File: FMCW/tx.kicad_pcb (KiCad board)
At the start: 2 copper layers, 125 x 45 mm, 70 parts, among them J1 Barrel_Jack, J2 SMA_RX, J3 SMA_TX, J4 Conn_01x06_Male, U1 ADF4158, U10 HMC431LP4, U2 LP2985-3.3, U3 TLV172DCK, U4 LM1117-5.0, U5 LP2985-10.0, U6 LP2985-3.0, U7 SE5003_1, U8 TCXO

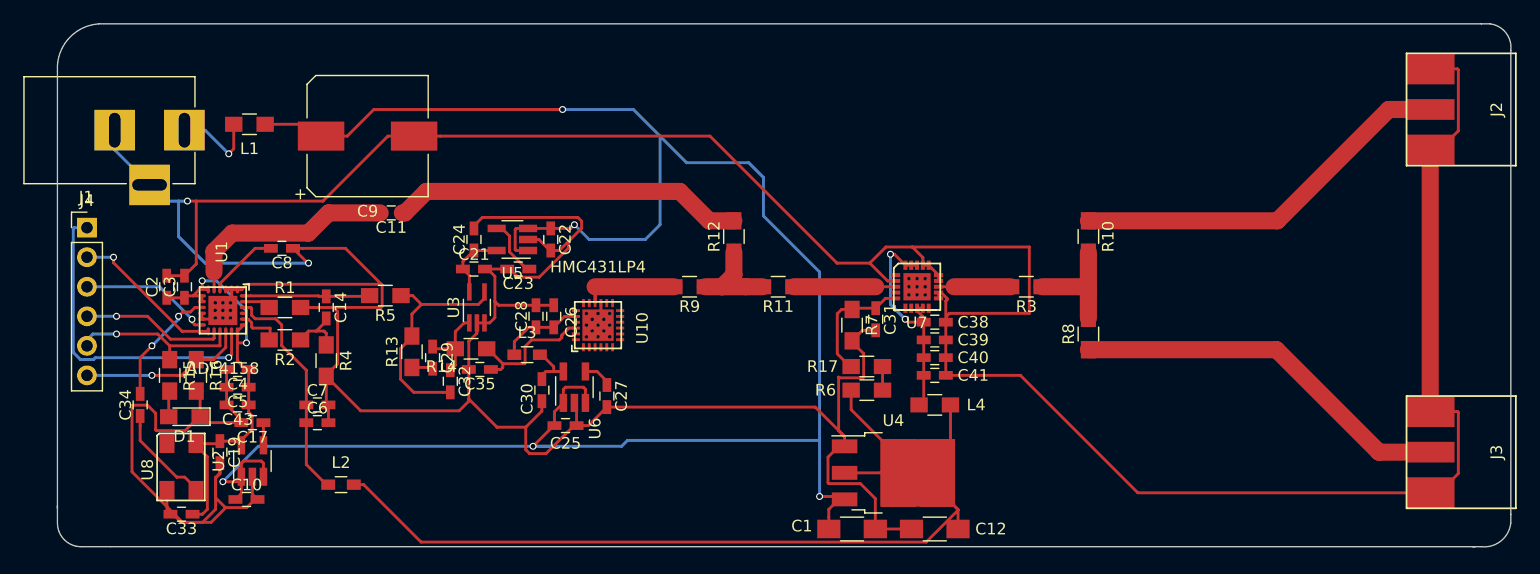
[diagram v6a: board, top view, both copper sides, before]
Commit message: Updated pcb with vias
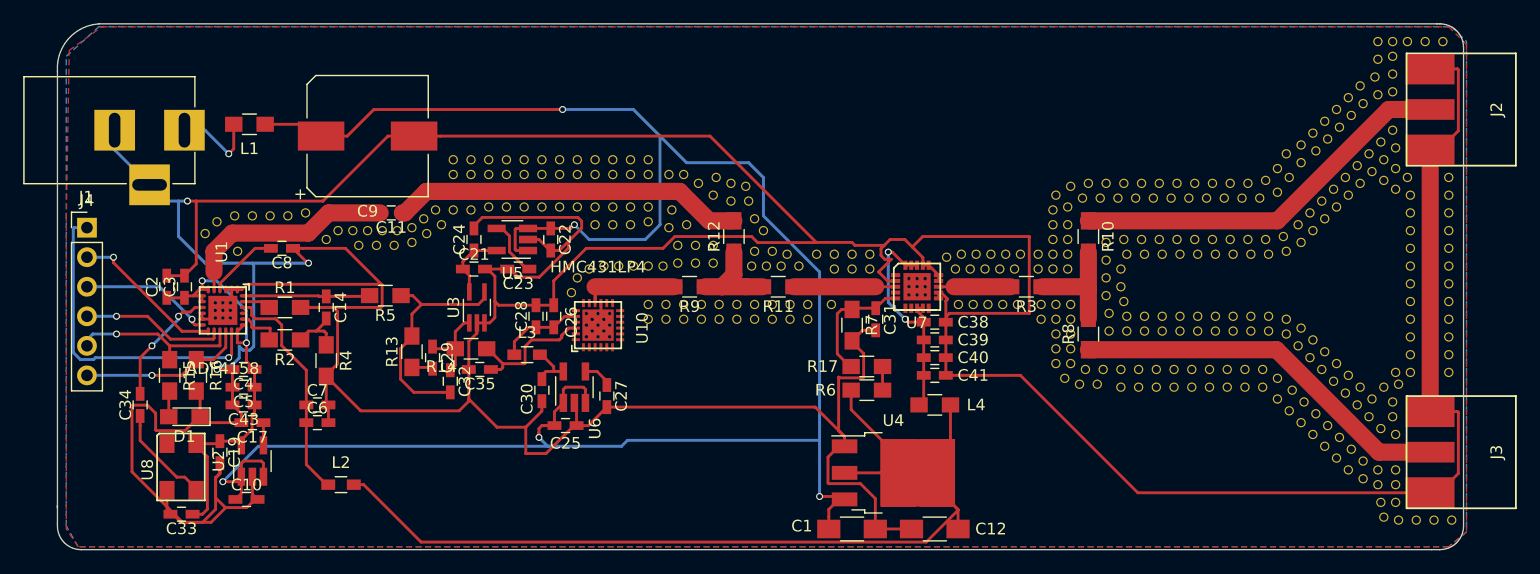
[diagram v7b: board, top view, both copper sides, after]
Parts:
- added REF**: VIA0.6mm, buradar:VIA0.6mm, F.Cu at (202.2, 91.2)
- added REF**: VIA0.6mm, buradar:VIA0.6mm, F.Cu at (190.2, 96.3)
- added REF**: VIA0.6mm, buradar:VIA0.6mm, F.Cu at (145.8, 97.3)
- added REF**: VIA0.6mm, buradar:VIA0.6mm, F.Cu at (147.1, 98.6)
- added REF**: VIA0.6mm, buradar:VIA0.6mm, F.Cu at (145.5, 98.8)
- added REF**: VIA0.6mm, buradar:VIA0.6mm, F.Cu at (150.9, 96.5)
- added REF**: VIA0.6mm, buradar:VIA0.6mm, F.Cu at (152.4, 96.5)
- added REF**: VIA0.6mm, buradar:VIA0.6mm, F.Cu at (149.6, 94.5)
- added REF**: VIA0.6mm, buradar:VIA0.6mm, F.Cu at (150.9, 95.0)
- added REF**: VIA0.6mm, buradar:VIA0.6mm, F.Cu at (152.1, 95.2)
- added REF**: VIA0.6mm, buradar:VIA0.6mm, F.Cu at (152.9, 98.0)
- added REF**: VIA0.6mm, buradar:VIA0.6mm, F.Cu at (153.7, 99.1)
- added REF**: VIA0.6mm, buradar:VIA0.6mm, F.Cu at (188.7, 96.3)
- added REF**: VIA0.6mm, buradar:VIA0.6mm, F.Cu at (152.9, 100.8)
- added REF**: VIA0.6mm, buradar:VIA0.6mm, F.Cu at (154.4, 100.8)
- added REF**: VIA0.6mm, buradar:VIA0.6mm, F.Cu at (156.7, 102.1)
- added REF**: VIA0.6mm, buradar:VIA0.6mm, F.Cu at (155.2, 102.1)
- added REF**: VIA0.6mm, buradar:VIA0.6mm, F.Cu at (153.9, 102.1)
- added REF**: VIA0.6mm, buradar:VIA0.6mm, F.Cu at (152.7, 102.1)
- added REF**: VIA0.6mm, buradar:VIA0.6mm, F.Cu at (155.7, 101.1)
- added REF**: VIA0.6mm, buradar:VIA0.6mm, F.Cu at (162.8, 102.4)
- added REF**: VIA0.6mm, buradar:VIA0.6mm, F.Cu at (161.3, 102.4)
- added REF**: VIA0.6mm, buradar:VIA0.6mm, F.Cu at (159.8, 102.4)
- added REF**: VIA0.6mm, buradar:VIA0.6mm, F.Cu at (187.2, 96.3)
- added REF**: VIA0.6mm, buradar:VIA0.6mm, F.Cu at (162.8, 101.1)
- added REF**: VIA0.6mm, buradar:VIA0.6mm, F.Cu at (161.3, 101.1)
- added REF**: VIA0.6mm, buradar:VIA0.6mm, F.Cu at (159.8, 101.1)
- added REF**: VIA0.6mm, buradar:VIA0.6mm, F.Cu at (158.2, 101.1)
- added REF**: VIA0.6mm, buradar:VIA0.6mm, F.Cu at (159.5, 105.4)
- added REF**: VIA0.6mm, buradar:VIA0.6mm, F.Cu at (157.5, 105.4)
- added REF**: VIA0.6mm, buradar:VIA0.6mm, F.Cu at (156.0, 105.4)
- added REF**: VIA0.6mm, buradar:VIA0.6mm, F.Cu at (154.4, 105.4)
- added REF**: VIA0.6mm, buradar:VIA0.6mm, F.Cu at (152.9, 105.4)
- added REF**: VIA0.6mm, buradar:VIA0.6mm, F.Cu at (151.4, 105.4)
- added REF**: VIA0.6mm, buradar:VIA0.6mm, F.Cu at (185.7, 96.3)
- added REF**: VIA0.6mm, buradar:VIA0.6mm, F.Cu at (149.9, 105.4)
- added REF**: VIA0.6mm, buradar:VIA0.6mm, F.Cu at (148.3, 105.4)
- added REF**: VIA0.6mm, buradar:VIA0.6mm, F.Cu at (146.8, 105.4)
- added REF**: VIA0.6mm, buradar:VIA0.6mm, F.Cu at (145.3, 105.4)
- added REF**: VIA0.6mm, buradar:VIA0.6mm, F.Cu at (143.8, 105.4)
- added REF**: VIA0.6mm, buradar:VIA0.6mm, F.Cu at (143.8, 106.7)
- added REF**: VIA0.6mm, buradar:VIA0.6mm, F.Cu at (145.3, 106.7)
- added REF**: VIA0.6mm, buradar:VIA0.6mm, F.Cu at (146.8, 106.7)
- added REF**: VIA0.6mm, buradar:VIA0.6mm, F.Cu at (148.3, 106.7)
- added REF**: VIA0.6mm, buradar:VIA0.6mm, F.Cu at (149.9, 106.7)
- added REF**: VIA0.6mm, buradar:VIA0.6mm, F.Cu at (184.2, 96.3)
- added REF**: VIA0.6mm, buradar:VIA0.6mm, F.Cu at (151.4, 106.7)
- added REF**: VIA0.6mm, buradar:VIA0.6mm, F.Cu at (152.9, 106.7)
- added REF**: VIA0.6mm, buradar:VIA0.6mm, F.Cu at (154.4, 106.7)
- added REF**: VIA0.6mm, buradar:VIA0.6mm, F.Cu at (156.0, 106.7)
- added REF**: VIA0.6mm, buradar:VIA0.6mm, F.Cu at (157.5, 106.7)
- added REF**: VIA0.6mm, buradar:VIA0.6mm, F.Cu at (170.2, 102.4)
- added REF**: VIA0.6mm, buradar:VIA0.6mm, F.Cu at (171.4, 102.4)
- added REF**: VIA0.6mm, buradar:VIA0.6mm, F.Cu at (172.7, 102.4)
- added REF**: VIA0.6mm, buradar:VIA0.6mm, F.Cu at (174.0, 102.4)
- added REF**: VIA0.6mm, buradar:VIA0.6mm, F.Cu at (175.3, 102.4)
- added REF**: VIA0.6mm, buradar:VIA0.6mm, F.Cu at (182.6, 96.3)
- added REF**: VIA0.6mm, buradar:VIA0.6mm, F.Cu at (169.4, 101.3)
- added REF**: VIA0.6mm, buradar:VIA0.6mm, F.Cu at (170.7, 101.1)
- added REF**: VIA0.6mm, buradar:VIA0.6mm, F.Cu at (172.0, 101.1)
- added REF**: VIA0.6mm, buradar:VIA0.6mm, F.Cu at (173.2, 101.1)
- added REF**: VIA0.6mm, buradar:VIA0.6mm, F.Cu at (174.5, 101.1)
- added REF**: VIA0.6mm, buradar:VIA0.6mm, F.Cu at (175.8, 101.1)
- added REF**: VIA0.6mm, buradar:VIA0.6mm, F.Cu at (170.4, 105.4)
- added REF**: VIA0.6mm, buradar:VIA0.6mm, F.Cu at (171.7, 105.4)
- added REF**: VIA0.6mm, buradar:VIA0.6mm, F.Cu at (173.0, 105.4)
- added REF**: VIA0.6mm, buradar:VIA0.6mm, F.Cu at (174.2, 105.4)
- added REF**: VIA0.6mm, buradar:VIA0.6mm, F.Cu at (181.1, 96.3)
- added REF**: VIA0.6mm, buradar:VIA0.6mm, F.Cu at (175.5, 105.4)
- added REF**: VIA0.6mm, buradar:VIA0.6mm, F.Cu at (177.3, 102.4)
- added REF**: VIA0.6mm, buradar:VIA0.6mm, F.Cu at (178.6, 102.4)
- added REF**: VIA0.6mm, buradar:VIA0.6mm, F.Cu at (179.8, 102.4)
- added REF**: VIA0.6mm, buradar:VIA0.6mm, F.Cu at (179.8, 101.1)
- added REF**: VIA0.6mm, buradar:VIA0.6mm, F.Cu at (178.6, 101.1)
- added REF**: VIA0.6mm, buradar:VIA0.6mm, F.Cu at (177.3, 101.1)
- added REF**: VIA0.6mm, buradar:VIA0.6mm, F.Cu at (179.8, 99.8)
- added REF**: VIA0.6mm, buradar:VIA0.6mm, F.Cu at (179.8, 98.6)
- added REF**: VIA0.6mm, buradar:VIA0.6mm, F.Cu at (179.8, 97.0)
- added REF**: VIA0.6mm, buradar:VIA0.6mm, F.Cu at (200.9, 90.7)
- added REF**: VIA0.6mm, buradar:VIA0.6mm, F.Cu at (178.6, 99.8)
- added REF**: VIA0.6mm, buradar:VIA0.6mm, F.Cu at (178.6, 98.6)
- added REF**: VIA0.6mm, buradar:VIA0.6mm, F.Cu at (178.6, 97.3)
- added REF**: VIA0.6mm, buradar:VIA0.6mm, F.Cu at (178.8, 96.0)
- added REF**: VIA0.6mm, buradar:VIA0.6mm, F.Cu at (149.4, 100.3)
- added REF**: VIA0.6mm, buradar:VIA0.6mm, F.Cu at (149.4, 101.9)
- added REF**: VIA0.6mm, buradar:VIA0.6mm, F.Cu at (147.8, 101.9)
- added REF**: VIA0.6mm, buradar:VIA0.6mm, F.Cu at (147.8, 100.3)
- added REF**: VIA0.6mm, buradar:VIA0.6mm, F.Cu at (146.3, 100.3)
- added REF**: VIA0.6mm, buradar:VIA0.6mm, F.Cu at (146.3, 101.9)
- added REF**: VIA0.6mm, buradar:VIA0.6mm, F.Cu at (199.9, 91.7)
- added REF**: VIA0.6mm, buradar:VIA0.6mm, F.Cu at (145.0, 102.1)
- added REF**: VIA0.6mm, buradar:VIA0.6mm, F.Cu at (143.8, 102.1)
- added REF**: VIA0.6mm, buradar:VIA0.6mm, F.Cu at (142.5, 102.1)
- added REF**: VIA0.6mm, buradar:VIA0.6mm, F.Cu at (141.2, 102.1)
- added REF**: VIA0.6mm, buradar:VIA0.6mm, F.Cu at (140.0, 102.1)
- added REF**: VIA0.6mm, buradar:VIA0.6mm, F.Cu at (138.7, 102.4)
- added REF**: VIA0.6mm, buradar:VIA0.6mm, F.Cu at (137.7, 103.1)
- added REF**: VIA0.6mm, buradar:VIA0.6mm, F.Cu at (137.2, 104.4)
- added REF**: VIA0.6mm, buradar:VIA0.6mm, F.Cu at (180.1, 105.4)
- added REF**: VIA0.6mm, buradar:VIA0.6mm, F.Cu at (178.8, 105.4)
- added REF**: VIA0.6mm, buradar:VIA0.6mm, F.Cu at (198.6, 92.5)
- added REF**: VIA0.6mm, buradar:VIA0.6mm, F.Cu at (177.5, 105.4)
- added REF**: VIA0.6mm, buradar:VIA0.6mm, F.Cu at (177.5, 106.7)
- added REF**: VIA0.6mm, buradar:VIA0.6mm, F.Cu at (178.8, 106.7)
- added REF**: VIA0.6mm, buradar:VIA0.6mm, F.Cu at (180.1, 106.7)
- added REF**: VIA0.6mm, buradar:VIA0.6mm, F.Cu at (180.1, 108.0)
- added REF**: VIA0.6mm, buradar:VIA0.6mm, F.Cu at (180.1, 109.2)
- added REF**: VIA0.6mm, buradar:VIA0.6mm, F.Cu at (180.1, 110.5)
- added REF**: VIA0.6mm, buradar:VIA0.6mm, F.Cu at (178.8, 108.0)
- added REF**: VIA0.6mm, buradar:VIA0.6mm, F.Cu at (178.8, 109.2)
- added REF**: VIA0.6mm, buradar:VIA0.6mm, F.Cu at (178.8, 110.5)
- added REF**: VIA0.6mm, buradar:VIA0.6mm, F.Cu at (201.2, 92.2)
- added REF**: VIA0.6mm, buradar:VIA0.6mm, F.Cu at (197.9, 93.7)
- added REF**: VIA0.6mm, buradar:VIA0.6mm, F.Cu at (181.4, 111.0)
- added REF**: VIA0.6mm, buradar:VIA0.6mm, F.Cu at (182.9, 111.0)
- added REF**: VIA0.6mm, buradar:VIA0.6mm, F.Cu at (179.6, 111.8)
- added REF**: VIA0.6mm, buradar:VIA0.6mm, F.Cu at (180.8, 112.3)
- added REF**: VIA0.6mm, buradar:VIA0.6mm, F.Cu at (182.4, 112.3)
- added REF**: VIA0.6mm, buradar:VIA0.6mm, F.Cu at (184.4, 111.0)
- added REF**: VIA0.6mm, buradar:VIA0.6mm, F.Cu at (185.9, 111.0)
- added REF**: VIA0.6mm, buradar:VIA0.6mm, F.Cu at (187.5, 111.0)
- added REF**: VIA0.6mm, buradar:VIA0.6mm, F.Cu at (189.0, 111.0)
- added REF**: VIA0.6mm, buradar:VIA0.6mm, F.Cu at (190.5, 111.0)
- added REF**: VIA0.6mm, buradar:VIA0.6mm, F.Cu at (196.8, 94.7)
- added REF**: VIA0.6mm, buradar:VIA0.6mm, F.Cu at (192.0, 111.0)
- added REF**: VIA0.6mm, buradar:VIA0.6mm, F.Cu at (193.5, 111.0)
- added REF**: VIA0.6mm, buradar:VIA0.6mm, F.Cu at (195.1, 111.0)
- added REF**: VIA0.6mm, buradar:VIA0.6mm, F.Cu at (196.6, 111.0)
- added REF**: VIA0.6mm, buradar:VIA0.6mm, F.Cu at (197.9, 111.8)
- added REF**: VIA0.6mm, buradar:VIA0.6mm, F.Cu at (199.1, 112.8)
- added REF**: VIA0.6mm, buradar:VIA0.6mm, F.Cu at (200.2, 113.8)
- added REF**: VIA0.6mm, buradar:VIA0.6mm, F.Cu at (201.2, 114.8)
- added REF**: VIA0.6mm, buradar:VIA0.6mm, F.Cu at (202.2, 115.8)
- added REF**: VIA0.6mm, buradar:VIA0.6mm, F.Cu at (203.2, 116.8)
- added REF**: VIA0.6mm, buradar:VIA0.6mm, F.Cu at (195.3, 95.0)
- added REF**: VIA0.6mm, buradar:VIA0.6mm, F.Cu at (204.2, 117.9)
- added REF**: VIA0.6mm, buradar:VIA0.6mm, F.Cu at (205.2, 118.9)
- added REF**: VIA0.6mm, buradar:VIA0.6mm, F.Cu at (206.5, 119.6)
- added REF**: VIA0.6mm, buradar:VIA0.6mm, F.Cu at (208.0, 119.6)
- added REF**: VIA0.6mm, buradar:VIA0.6mm, F.Cu at (208.0, 120.9)
- added REF**: VIA0.6mm, buradar:VIA0.6mm, F.Cu at (206.5, 120.9)
- added REF**: VIA0.6mm, buradar:VIA0.6mm, F.Cu at (205.2, 120.4)
- added REF**: VIA0.6mm, buradar:VIA0.6mm, F.Cu at (204.0, 119.6)
- added REF**: VIA0.6mm, buradar:VIA0.6mm, F.Cu at (202.9, 118.6)
- added REF**: VIA0.6mm, buradar:VIA0.6mm, F.Cu at (201.9, 117.6)
- added REF**: VIA0.6mm, buradar:VIA0.6mm, F.Cu at (193.8, 95.0)
- added REF**: VIA0.6mm, buradar:VIA0.6mm, F.Cu at (200.9, 116.6)
- added REF**: VIA0.6mm, buradar:VIA0.6mm, F.Cu at (199.9, 115.6)
- added REF**: VIA0.6mm, buradar:VIA0.6mm, F.Cu at (198.9, 114.6)
- added REF**: VIA0.6mm, buradar:VIA0.6mm, F.Cu at (197.9, 113.5)
- added REF**: VIA0.6mm, buradar:VIA0.6mm, F.Cu at (196.6, 112.5)
- added REF**: VIA0.6mm, buradar:VIA0.6mm, F.Cu at (195.1, 112.5)
- added REF**: VIA0.6mm, buradar:VIA0.6mm, F.Cu at (193.5, 112.5)
- added REF**: VIA0.6mm, buradar:VIA0.6mm, F.Cu at (192.0, 112.5)
- added REF**: VIA0.6mm, buradar:VIA0.6mm, F.Cu at (190.5, 112.5)
- added REF**: VIA0.6mm, buradar:VIA0.6mm, F.Cu at (189.0, 112.5)
- added REF**: VIA0.6mm, buradar:VIA0.6mm, F.Cu at (192.3, 95.0)
- added REF**: VIA0.6mm, buradar:VIA0.6mm, F.Cu at (187.5, 112.5)
- added REF**: VIA0.6mm, buradar:VIA0.6mm, F.Cu at (185.9, 112.5)
- added REF**: VIA0.6mm, buradar:VIA0.6mm, F.Cu at (184.4, 112.5)
- added REF**: VIA0.6mm, buradar:VIA0.6mm, F.Cu at (203.2, 90.2)
- added REF**: VIA0.6mm, buradar:VIA0.6mm, F.Cu at (204.2, 89.2)
- added REF**: VIA0.6mm, buradar:VIA0.6mm, F.Cu at (205.2, 88.1)
- added REF**: VIA0.6mm, buradar:VIA0.6mm, F.Cu at (206.5, 87.4)
- added REF**: VIA0.6mm, buradar:VIA0.6mm, F.Cu at (207.8, 87.1)
- added REF**: VIA0.6mm, buradar:VIA0.6mm, F.Cu at (212.1, 82.8)
- added REF**: VIA0.6mm, buradar:VIA0.6mm, F.Cu at (210.6, 82.8)
- added REF**: VIA0.6mm, buradar:VIA0.6mm, F.Cu at (190.8, 95.0)
- added REF**: VIA0.6mm, buradar:VIA0.6mm, F.Cu at (209.0, 82.8)
- added REF**: VIA0.6mm, buradar:VIA0.6mm, F.Cu at (201.9, 89.7)
- added REF**: VIA0.6mm, buradar:VIA0.6mm, F.Cu at (202.9, 88.6)
- added REF**: VIA0.6mm, buradar:VIA0.6mm, F.Cu at (204.0, 87.6)
- added REF**: VIA0.6mm, buradar:VIA0.6mm, F.Cu at (205.0, 86.6)
- added REF**: VIA0.6mm, buradar:VIA0.6mm, F.Cu at (206.2, 85.9)
- added REF**: VIA0.6mm, buradar:VIA0.6mm, F.Cu at (207.8, 85.6)
- added REF**: VIA0.6mm, buradar:VIA0.6mm, F.Cu at (207.8, 84.1)
- added REF**: VIA0.6mm, buradar:VIA0.6mm, F.Cu at (207.8, 82.8)
- added REF**: VIA0.6mm, buradar:VIA0.6mm, F.Cu at (206.5, 84.3)
- added REF**: VIA0.6mm, buradar:VIA0.6mm, F.Cu at (189.2, 95.0)
- added REF**: VIA0.6mm, buradar:VIA0.6mm, F.Cu at (206.5, 82.8)
- added REF**: VIA0.6mm, buradar:VIA0.6mm, F.Cu at (208.0, 122.4)
- added REF**: VIA0.6mm, buradar:VIA0.6mm, F.Cu at (212.9, 124.0)
- added REF**: VIA0.6mm, buradar:VIA0.6mm, F.Cu at (211.3, 124.0)
- added REF**: VIA0.6mm, buradar:VIA0.6mm, F.Cu at (209.8, 124.0)
- added REF**: VIA0.6mm, buradar:VIA0.6mm, F.Cu at (208.3, 124.0)
- added REF**: VIA0.6mm, buradar:VIA0.6mm, F.Cu at (206.8, 122.4)
- added REF**: VIA0.6mm, buradar:VIA0.6mm, F.Cu at (207.0, 123.7)
- added REF**: VIA0.6mm, buradar:VIA0.6mm, F.Cu at (212.6, 94.5)
- added REF**: VIA0.6mm, buradar:VIA0.6mm, F.Cu at (212.6, 96.0)
- added REF**: VIA0.6mm, buradar:VIA0.6mm, F.Cu at (187.7, 95.0)
- added REF**: VIA0.6mm, buradar:VIA0.6mm, F.Cu at (212.6, 97.5)
- added REF**: VIA0.6mm, buradar:VIA0.6mm, F.Cu at (212.6, 99.1)
- added REF**: VIA0.6mm, buradar:VIA0.6mm, F.Cu at (212.6, 100.6)
- added REF**: VIA0.6mm, buradar:VIA0.6mm, F.Cu at (212.6, 102.1)
- added REF**: VIA0.6mm, buradar:VIA0.6mm, F.Cu at (212.6, 103.6)
- added REF**: VIA0.6mm, buradar:VIA0.6mm, F.Cu at (212.6, 105.2)
- added REF**: VIA0.6mm, buradar:VIA0.6mm, F.Cu at (212.6, 106.7)
- added REF**: VIA0.6mm, buradar:VIA0.6mm, F.Cu at (212.6, 108.2)
- added REF**: VIA0.6mm, buradar:VIA0.6mm, F.Cu at (212.6, 109.7)
- added REF**: VIA0.6mm, buradar:VIA0.6mm, F.Cu at (212.6, 111.3)
- added REF**: VIA0.6mm, buradar:VIA0.6mm, F.Cu at (186.2, 95.0)
- added REF**: VIA0.6mm, buradar:VIA0.6mm, F.Cu at (207.8, 90.4)
- added REF**: VIA0.6mm, buradar:VIA0.6mm, F.Cu at (208.0, 91.9)
- added REF**: VIA0.6mm, buradar:VIA0.6mm, F.Cu at (207.0, 93.0)
- added REF**: VIA0.6mm, buradar:VIA0.6mm, F.Cu at (209.0, 94.5)
- added REF**: VIA0.6mm, buradar:VIA0.6mm, F.Cu at (209.3, 96.0)
- added REF**: VIA0.6mm, buradar:VIA0.6mm, F.Cu at (209.3, 97.5)
- added REF**: VIA0.6mm, buradar:VIA0.6mm, F.Cu at (209.3, 99.1)
- added REF**: VIA0.6mm, buradar:VIA0.6mm, F.Cu at (209.3, 100.6)
- added REF**: VIA0.6mm, buradar:VIA0.6mm, F.Cu at (209.3, 102.1)
- added REF**: VIA0.6mm, buradar:VIA0.6mm, F.Cu at (209.3, 103.6)
- added REF**: VIA0.6mm, buradar:VIA0.6mm, F.Cu at (184.7, 95.0)
- added REF**: VIA0.6mm, buradar:VIA0.6mm, F.Cu at (209.3, 105.2)
- added REF**: VIA0.6mm, buradar:VIA0.6mm, F.Cu at (209.3, 106.7)
- added REF**: VIA0.6mm, buradar:VIA0.6mm, F.Cu at (209.3, 108.2)
- added REF**: VIA0.6mm, buradar:VIA0.6mm, F.Cu at (209.3, 109.7)
- added REF**: VIA0.6mm, buradar:VIA0.6mm, F.Cu at (209.3, 111.3)
- added REF**: VIA0.6mm, buradar:VIA0.6mm, F.Cu at (208.3, 112.3)
- added REF**: VIA0.6mm, buradar:VIA0.6mm, F.Cu at (207.8, 113.8)
- added REF**: VIA0.6mm, buradar:VIA0.6mm, F.Cu at (207.8, 115.1)
- added REF**: VIA0.6mm, buradar:VIA0.6mm, F.Cu at (208.0, 116.6)
- added REF**: VIA0.6mm, buradar:VIA0.6mm, F.Cu at (206.8, 116.1)
- added REF**: VIA0.6mm, buradar:VIA0.6mm, F.Cu at (199.9, 93.2)
- added REF**: VIA0.6mm, buradar:VIA0.6mm, F.Cu at (183.1, 95.0)
- added REF**: VIA0.6mm, buradar:VIA0.6mm, F.Cu at (205.7, 115.1)
- added REF**: VIA0.6mm, buradar:VIA0.6mm, F.Cu at (204.7, 114.0)
- added REF**: VIA0.6mm, buradar:VIA0.6mm, F.Cu at (203.7, 113.0)
- added REF**: VIA0.6mm, buradar:VIA0.6mm, F.Cu at (202.7, 112.0)
- added REF**: VIA0.6mm, buradar:VIA0.6mm, F.Cu at (201.7, 111.0)
- added REF**: VIA0.6mm, buradar:VIA0.6mm, F.Cu at (200.7, 110.0)
- added REF**: VIA0.6mm, buradar:VIA0.6mm, F.Cu at (199.6, 109.0)
- added REF**: VIA0.6mm, buradar:VIA0.6mm, F.Cu at (198.6, 108.0)
- added REF**: VIA0.6mm, buradar:VIA0.6mm, F.Cu at (197.1, 107.7)
- added REF**: VIA0.6mm, buradar:VIA0.6mm, F.Cu at (195.6, 107.7)
- added REF**: VIA0.6mm, buradar:VIA0.6mm, F.Cu at (181.6, 95.0)
- added REF**: VIA0.6mm, buradar:VIA0.6mm, F.Cu at (194.1, 107.7)
- added REF**: VIA0.6mm, buradar:VIA0.6mm, F.Cu at (192.5, 107.7)
- added REF**: VIA0.6mm, buradar:VIA0.6mm, F.Cu at (191.0, 107.7)
- added REF**: VIA0.6mm, buradar:VIA0.6mm, F.Cu at (189.5, 107.7)
- added REF**: VIA0.6mm, buradar:VIA0.6mm, F.Cu at (188.0, 107.7)
- added REF**: VIA0.6mm, buradar:VIA0.6mm, F.Cu at (186.4, 107.7)
- added REF**: VIA0.6mm, buradar:VIA0.6mm, F.Cu at (184.9, 107.7)
- added REF**: VIA0.6mm, buradar:VIA0.6mm, F.Cu at (183.4, 107.7)
- added REF**: VIA0.6mm, buradar:VIA0.6mm, F.Cu at (183.4, 106.2)
- added REF**: VIA0.6mm, buradar:VIA0.6mm, F.Cu at (183.1, 104.6)
- added REF**: VIA0.6mm, buradar:VIA0.6mm, F.Cu at (180.1, 95.2)
- added REF**: VIA0.6mm, buradar:VIA0.6mm, F.Cu at (183.1, 103.1)
- added REF**: VIA0.6mm, buradar:VIA0.6mm, F.Cu at (183.1, 101.6)
- added REF**: VIA0.6mm, buradar:VIA0.6mm, F.Cu at (183.1, 100.1)
- added REF**: VIA0.6mm, buradar:VIA0.6mm, F.Cu at (184.7, 99.8)
- added REF**: VIA0.6mm, buradar:VIA0.6mm, F.Cu at (186.2, 99.8)
- added REF**: VIA0.6mm, buradar:VIA0.6mm, F.Cu at (187.7, 99.8)
- added REF**: VIA0.6mm, buradar:VIA0.6mm, F.Cu at (189.2, 99.8)
- added REF**: VIA0.6mm, buradar:VIA0.6mm, F.Cu at (190.8, 99.8)
- added REF**: VIA0.6mm, buradar:VIA0.6mm, F.Cu at (192.3, 99.8)
- added REF**: VIA0.6mm, buradar:VIA0.6mm, F.Cu at (193.8, 99.8)
- added REF**: VIA0.6mm, buradar:VIA0.6mm, F.Cu at (149.4, 96.0)
- added REF**: VIA0.6mm, buradar:VIA0.6mm, F.Cu at (195.3, 99.8)
- added REF**: VIA0.6mm, buradar:VIA0.6mm, F.Cu at (196.8, 99.8)
- added REF**: VIA0.6mm, buradar:VIA0.6mm, F.Cu at (198.4, 99.6)
- added REF**: VIA0.6mm, buradar:VIA0.6mm, F.Cu at (199.6, 98.6)
- added REF**: VIA0.6mm, buradar:VIA0.6mm, F.Cu at (200.7, 97.5)
- added REF**: VIA0.6mm, buradar:VIA0.6mm, F.Cu at (201.7, 96.5)
- added REF**: VIA0.6mm, buradar:VIA0.6mm, F.Cu at (202.7, 95.5)
- added REF**: VIA0.6mm, buradar:VIA0.6mm, F.Cu at (203.7, 94.5)
- added REF**: VIA0.6mm, buradar:VIA0.6mm, F.Cu at (204.7, 93.5)
- added REF**: VIA0.6mm, buradar:VIA0.6mm, F.Cu at (205.7, 92.5)
- added REF**: VIA0.6mm, buradar:VIA0.6mm, F.Cu at (148.1, 95.0)
- added REF**: VIA0.6mm, buradar:VIA0.6mm, F.Cu at (206.8, 91.4)
- added REF**: VIA0.6mm, buradar:VIA0.6mm, F.Cu at (206.0, 94.0)
- added REF**: VIA0.6mm, buradar:VIA0.6mm, F.Cu at (205.0, 95.0)
- added REF**: VIA0.6mm, buradar:VIA0.6mm, F.Cu at (204.0, 96.0)
- added REF**: VIA0.6mm, buradar:VIA0.6mm, F.Cu at (208.0, 93.7)
- added REF**: VIA0.6mm, buradar:VIA0.6mm, F.Cu at (207.0, 94.7)
- added REF**: VIA0.6mm, buradar:VIA0.6mm, F.Cu at (208.0, 95.5)
- added REF**: VIA0.6mm, buradar:VIA0.6mm, F.Cu at (202.9, 97.0)
- added REF**: VIA0.6mm, buradar:VIA0.6mm, F.Cu at (201.9, 98.0)
- added REF**: VIA0.6mm, buradar:VIA0.6mm, F.Cu at (200.9, 99.1)
- added REF**: VIA0.6mm, buradar:VIA0.6mm, F.Cu at (146.8, 94.2)
- added REF**: VIA0.6mm, buradar:VIA0.6mm, F.Cu at (199.9, 100.1)
- added REF**: VIA0.6mm, buradar:VIA0.6mm, F.Cu at (198.6, 100.8)
- added REF**: VIA0.6mm, buradar:VIA0.6mm, F.Cu at (197.1, 101.1)
- added REF**: VIA0.6mm, buradar:VIA0.6mm, F.Cu at (195.6, 101.1)
- added REF**: VIA0.6mm, buradar:VIA0.6mm, F.Cu at (194.1, 101.1)
- added REF**: VIA0.6mm, buradar:VIA0.6mm, F.Cu at (192.5, 101.1)
- added REF**: VIA0.6mm, buradar:VIA0.6mm, F.Cu at (191.0, 101.1)
- added REF**: VIA0.6mm, buradar:VIA0.6mm, F.Cu at (189.5, 101.1)
- added REF**: VIA0.6mm, buradar:VIA0.6mm, F.Cu at (188.0, 101.1)
- added REF**: VIA0.6mm, buradar:VIA0.6mm, F.Cu at (186.4, 101.1)
- added REF**: VIA0.6mm, buradar:VIA0.6mm, F.Cu at (145.5, 94.2)
- added REF**: VIA0.6mm, buradar:VIA0.6mm, F.Cu at (184.9, 101.1)
- added REF**: VIA0.6mm, buradar:VIA0.6mm, F.Cu at (184.4, 102.4)
- added REF**: VIA0.6mm, buradar:VIA0.6mm, F.Cu at (184.4, 103.9)
- added REF**: VIA0.6mm, buradar:VIA0.6mm, F.Cu at (184.7, 105.2)
- added REF**: VIA0.6mm, buradar:VIA0.6mm, F.Cu at (184.9, 106.4)
- added REF**: VIA0.6mm, buradar:VIA0.6mm, F.Cu at (186.4, 106.4)
- added REF**: VIA0.6mm, buradar:VIA0.6mm, F.Cu at (188.0, 106.4)
- added REF**: VIA0.6mm, buradar:VIA0.6mm, F.Cu at (189.5, 106.4)
- added REF**: VIA0.6mm, buradar:VIA0.6mm, F.Cu at (191.0, 106.4)
- added REF**: VIA0.6mm, buradar:VIA0.6mm, F.Cu at (192.5, 106.4)
- added REF**: VIA0.6mm, buradar:VIA0.6mm, F.Cu at (143.8, 94.2)
- added REF**: VIA0.6mm, buradar:VIA0.6mm, F.Cu at (194.1, 106.4)
- added REF**: VIA0.6mm, buradar:VIA0.6mm, F.Cu at (195.6, 106.4)
- added REF**: VIA0.6mm, buradar:VIA0.6mm, F.Cu at (197.1, 106.4)
- added REF**: VIA0.6mm, buradar:VIA0.6mm, F.Cu at (198.6, 106.7)
- added REF**: VIA0.6mm, buradar:VIA0.6mm, F.Cu at (199.9, 107.4)
- added REF**: VIA0.6mm, buradar:VIA0.6mm, F.Cu at (200.9, 108.5)
- added REF**: VIA0.6mm, buradar:VIA0.6mm, F.Cu at (201.9, 109.5)
- added REF**: VIA0.6mm, buradar:VIA0.6mm, F.Cu at (202.9, 110.5)
- added REF**: VIA0.6mm, buradar:VIA0.6mm, F.Cu at (204.0, 111.5)
- added REF**: VIA0.6mm, buradar:VIA0.6mm, F.Cu at (205.0, 112.5)
- added REF**: VIA0.6mm, buradar:VIA0.6mm, F.Cu at (142.2, 94.2)
- added REF**: VIA0.6mm, buradar:VIA0.6mm, F.Cu at (206.0, 113.5)
- added REF**: VIA0.6mm, buradar:VIA0.6mm, F.Cu at (207.0, 112.5)
- added REF**: VIA0.6mm, buradar:VIA0.6mm, F.Cu at (208.0, 111.3)
- added REF**: VIA0.6mm, buradar:VIA0.6mm, F.Cu at (140.7, 94.2)
- added REF**: VIA0.6mm, buradar:VIA0.6mm, F.Cu at (198.9, 94.5)
- added REF**: VIA0.6mm, buradar:VIA0.6mm, F.Cu at (139.2, 94.2)
- added REF**: VIA0.6mm, buradar:VIA0.6mm, F.Cu at (137.7, 94.2)
- added REF**: VIA0.6mm, buradar:VIA0.6mm, F.Cu at (136.1, 94.2)
- added REF**: VIA0.6mm, buradar:VIA0.6mm, F.Cu at (134.6, 94.2)
- added REF**: VIA0.6mm, buradar:VIA0.6mm, F.Cu at (133.1, 94.2)
- added REF**: VIA0.6mm, buradar:VIA0.6mm, F.Cu at (131.6, 94.2)
- added REF**: VIA0.6mm, buradar:VIA0.6mm, F.Cu at (130.0, 94.2)
- added REF**: VIA0.6mm, buradar:VIA0.6mm, F.Cu at (128.5, 94.2)
- added REF**: VIA0.6mm, buradar:VIA0.6mm, F.Cu at (127.0, 94.2)
- added REF**: VIA0.6mm, buradar:VIA0.6mm, F.Cu at (105.7, 99.3)
- added REF**: VIA0.6mm, buradar:VIA0.6mm, F.Cu at (197.9, 95.8)
- added REF**: VIA0.6mm, buradar:VIA0.6mm, F.Cu at (106.7, 98.3)
- added REF**: VIA0.6mm, buradar:VIA0.6mm, F.Cu at (108.5, 100.8)
- added REF**: VIA0.6mm, buradar:VIA0.6mm, F.Cu at (108.2, 97.8)
- added REF**: VIA0.6mm, buradar:VIA0.6mm, F.Cu at (109.7, 97.8)
- added REF**: VIA0.6mm, buradar:VIA0.6mm, F.Cu at (111.3, 97.8)
- added REF**: VIA0.6mm, buradar:VIA0.6mm, F.Cu at (112.8, 97.8)
- added REF**: VIA0.6mm, buradar:VIA0.6mm, F.Cu at (114.3, 97.5)
- added REF**: VIA0.6mm, buradar:VIA0.6mm, F.Cu at (116.1, 99.8)
- added REF**: VIA0.6mm, buradar:VIA0.6mm, F.Cu at (117.1, 99.1)
- added REF**: VIA0.6mm, buradar:VIA0.6mm, F.Cu at (118.4, 99.1)
- added REF**: VIA0.6mm, buradar:VIA0.6mm, F.Cu at (196.3, 96.3)
- added REF**: VIA0.6mm, buradar:VIA0.6mm, F.Cu at (119.6, 99.1)
- added REF**: VIA0.6mm, buradar:VIA0.6mm, F.Cu at (120.9, 99.1)
- added REF**: VIA0.6mm, buradar:VIA0.6mm, F.Cu at (122.2, 99.1)
- added REF**: VIA0.6mm, buradar:VIA0.6mm, F.Cu at (123.4, 98.8)
- added REF**: VIA0.6mm, buradar:VIA0.6mm, F.Cu at (124.5, 98.0)
- added REF**: VIA0.6mm, buradar:VIA0.6mm, F.Cu at (125.5, 97.3)
- added REF**: VIA0.6mm, buradar:VIA0.6mm, F.Cu at (127.0, 97.3)
- added REF**: VIA0.6mm, buradar:VIA0.6mm, F.Cu at (128.5, 97.3)
- added REF**: VIA0.6mm, buradar:VIA0.6mm, F.Cu at (130.0, 97.0)
- added REF**: VIA0.6mm, buradar:VIA0.6mm, F.Cu at (131.6, 97.0)
- added REF**: VIA0.6mm, buradar:VIA0.6mm, F.Cu at (194.8, 96.3)
- added REF**: VIA0.6mm, buradar:VIA0.6mm, F.Cu at (133.1, 97.0)
- added REF**: VIA0.6mm, buradar:VIA0.6mm, F.Cu at (134.6, 97.0)
- added REF**: VIA0.6mm, buradar:VIA0.6mm, F.Cu at (136.1, 97.0)
- added REF**: VIA0.6mm, buradar:VIA0.6mm, F.Cu at (137.7, 97.0)
- added REF**: VIA0.6mm, buradar:VIA0.6mm, F.Cu at (139.2, 97.0)
- added REF**: VIA0.6mm, buradar:VIA0.6mm, F.Cu at (140.7, 97.0)
- added REF**: VIA0.6mm, buradar:VIA0.6mm, F.Cu at (142.2, 97.0)
- added REF**: VIA0.6mm, buradar:VIA0.6mm, F.Cu at (143.8, 97.0)
- added REF**: VIA0.6mm, buradar:VIA0.6mm, F.Cu at (143.8, 98.3)
- added REF**: VIA0.6mm, buradar:VIA0.6mm, F.Cu at (142.2, 98.6)
- added REF**: VIA0.6mm, buradar:VIA0.6mm, F.Cu at (193.3, 96.3)
- added REF**: VIA0.6mm, buradar:VIA0.6mm, F.Cu at (140.7, 98.6)
- added REF**: VIA0.6mm, buradar:VIA0.6mm, F.Cu at (139.2, 98.6)
- added REF**: VIA0.6mm, buradar:VIA0.6mm, F.Cu at (118.9, 100.3)
- added REF**: VIA0.6mm, buradar:VIA0.6mm, F.Cu at (120.4, 100.3)
- added REF**: VIA0.6mm, buradar:VIA0.6mm, F.Cu at (121.9, 100.3)
- added REF**: VIA0.6mm, buradar:VIA0.6mm, F.Cu at (123.4, 100.1)
- added REF**: VIA0.6mm, buradar:VIA0.6mm, F.Cu at (124.7, 99.3)
- added REF**: VIA0.6mm, buradar:VIA0.6mm, F.Cu at (126.0, 98.6)
- added REF**: VIA0.6mm, buradar:VIA0.6mm, F.Cu at (127.0, 93.0)
- added REF**: VIA0.6mm, buradar:VIA0.6mm, F.Cu at (128.5, 93.0)
- added REF**: VIA0.6mm, buradar:VIA0.6mm, F.Cu at (191.8, 96.3)
- added REF**: VIA0.6mm, buradar:VIA0.6mm, F.Cu at (130.0, 93.0)
- added REF**: VIA0.6mm, buradar:VIA0.6mm, F.Cu at (131.6, 93.0)
- added REF**: VIA0.6mm, buradar:VIA0.6mm, F.Cu at (133.1, 93.0)
- added REF**: VIA0.6mm, buradar:VIA0.6mm, F.Cu at (134.6, 93.0)
- added REF**: VIA0.6mm, buradar:VIA0.6mm, F.Cu at (136.1, 93.0)
- added REF**: VIA0.6mm, buradar:VIA0.6mm, F.Cu at (137.7, 93.0)
- added REF**: VIA0.6mm, buradar:VIA0.6mm, F.Cu at (139.2, 93.0)
- added REF**: VIA0.6mm, buradar:VIA0.6mm, F.Cu at (140.7, 93.0)
- added REF**: VIA0.6mm, buradar:VIA0.6mm, F.Cu at (142.2, 93.0)
- added REF**: VIA0.6mm, buradar:VIA0.6mm, F.Cu at (143.8, 93.0)
- moved C4 0.51 mm to (109.0, 111.0)
- moved C43 0.51 mm to (109.0, 114.0)
- moved C5 0.51 mm to (109.0, 112.5)
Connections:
- U7 pad GND: (no net) -> GND
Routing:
- net GND: track 473.5 -> 516.7 mm, vias 2 -> 3
- net Net-(C38-Pad2): track 19.7 -> 20.2 mm
- added copper zone on B.Cu, net GND
- added copper zone on F.Cu, net GND
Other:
- board size 125 x 45 mm -> 120.9 x 45.2 mm
